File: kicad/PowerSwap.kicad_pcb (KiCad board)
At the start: 2 copper layers, 23.9 x 18.6 mm, 58 parts, among them P1 Battery, P2 Vout, P3 TST, P4 TST, P5 TST, P6 TST, P7 TST, P8 TST, P9 TST, U1 TPS63030

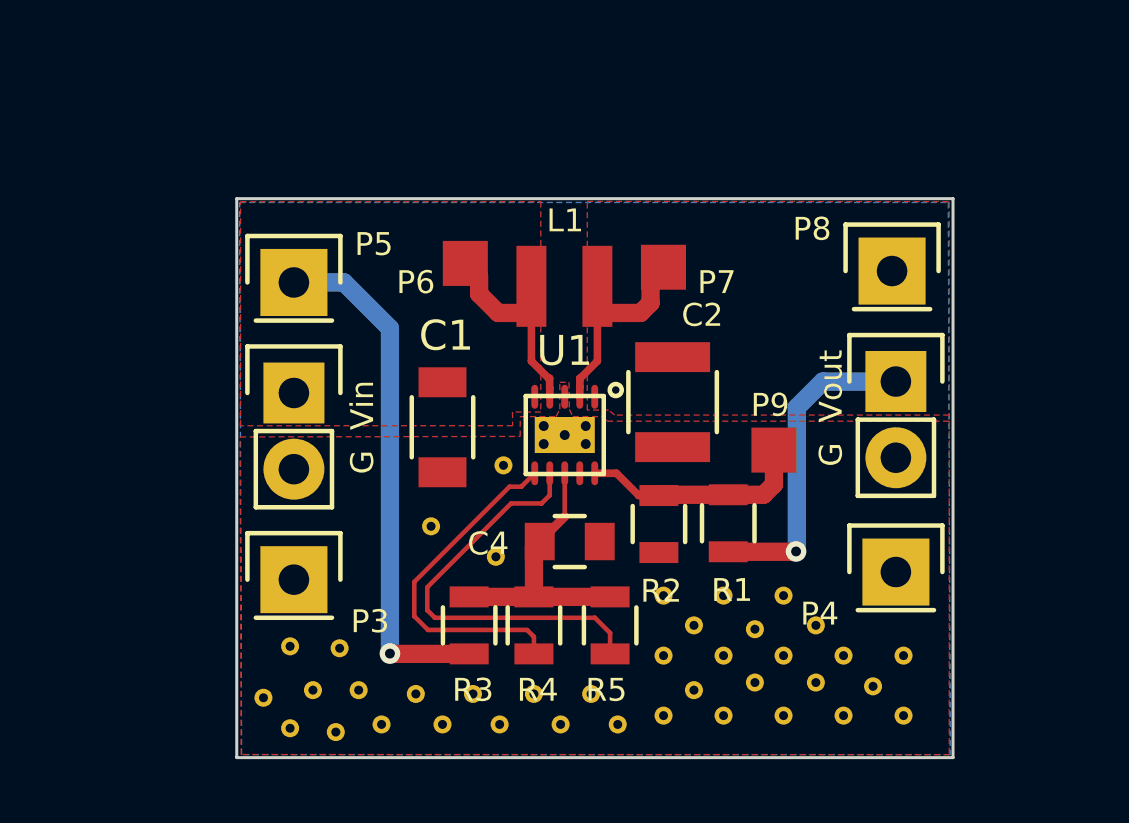
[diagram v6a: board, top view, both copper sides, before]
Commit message: Added tracks to GND of the TPS63030
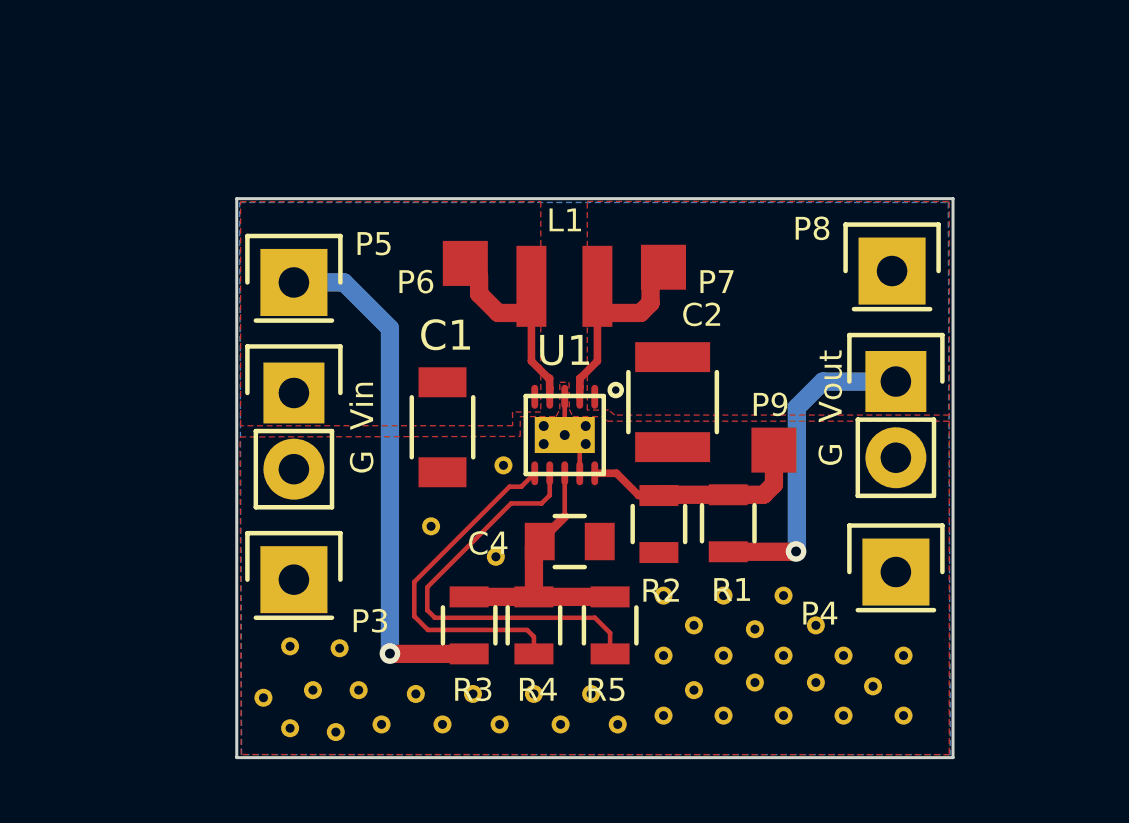
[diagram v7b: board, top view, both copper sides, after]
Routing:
- net GNDPWR: track 0.00 -> 2.76 mm
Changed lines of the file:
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@@
     (thickness 1.6)
     (drawings 7)
-    (tracks 62)
+    (tracks 65)
     (zones 0)
     (modules 58)
@@
   )
   (setup
-    (last_trace_width 0.6096)
+    (last_trace_width 0.1524)
     (user_trace_width 0.3048)
     (user_trace_width 0.6096)
@@
   (via (at 139.9794 102.0318) (size 0.6858) (drill 0.3302) (layers F.Cu B.Cu) (net 1))
   (segment (start 139.9896 102.042) (end 139.9794 102.0318) (width 0.6096) (layer F.Cu) (net 1))
+  (segment (start 146.3072 96.0218) (end 146.3072 95.2468) (width 0.1524) (layer F.Cu) (net 2) (status C00000))
+  (segment (start 146.3072 95.2468) (end 145.8072 94.7468) (width 0.1524) (layer F.Cu) (net 2) (status C00000))
+  (segment (start 145.8072 93.4718) (end 145.8072 94.7468) (width 0.1524) (layer F.Cu) (net 2) (status C00000))
   (segment (start 151.257 98.6384) (end 153.5074 98.6384) (width 0.6096) (layer F.Cu) (net 3))
   (segment (start 154.4066 92.964) (end 156.845 92.964) (width 0.6096) (layer B.Cu) (net 3))
@@
   (via (at 153.5176 98.6282) (size 0.6858) (drill 0.3302) (layers F.Cu B.Cu) (net 3))
   (segment (start 153.5074 98.6384) (end 153.5176 98.6282) (width 0.6096) (layer F.Cu) (net 3))
-  (segment (start 151.257 96.7384) (end 152.4356 96.7384) (width 0.6096) (layer F.Cu) (net 4) (status 400000))
-  (segment (start 152.781 96.393) (end 152.781 95.25) (width 0.6096) (layer F.Cu) (net 4) (status 800000))
+  (segment (start 151.257 96.7384) (end 152.4356 96.7384) (width 0.6096) (layer F.Cu) (net 4))
+  (segment (start 152.781 96.393) (end 152.781 95.25) (width 0.6096) (layer F.Cu) (net 4))
   (segment (start 152.4356 96.7384) (end 152.781 96.393) (width 0.6096) (layer F.Cu) (net 4))
   (segment (start 148.9456 96.7638) (end 148.275 96.7638) (width 0.254) (layer F.Cu) (net 4))
